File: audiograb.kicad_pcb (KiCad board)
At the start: 4 copper layers, 166.6 x 68.9 mm, 105 parts, among them IC1 USB2244I-AEZG-06, J1 USB_C_Receptacle_USB2.0_16P, J10 TestPoint, J11 TestPoint, J12 TestPoint, J13 TestPoint, J14 TestPoint, J15 F32Q-1A7H1-11022, J16 MEM2075-00-140-01-A, J17 5V_out, J18 3V7_in, J19 3V3_in, J2 SAM10346-ND, J3 Conn_02x20_Odd_Even, J4 CONMHF1-SMD-G-T, J5 CONMHF1-SMD-G-T, J6 TestPoint, J7 TestPoint, J8 TestPoint, J9 TestPoint, M1 ComputeModule5-CM5, P1 SF72S006VBAR2500, Q1 Q_PMOS_GSD, SW1 1825910-6, U1 RC7620_1104625, U10 CD4043BDR, U11 TPS22919DCKR, U12 IP4220CZ6F, U2 NX3008NBKW_115, U3 NX3008NBKW_115, U4 NX3008NBKW_115, U5 NX3008NBKW_115, U6 NX3008NBKW_115, U7 NX3008NBKW_115, U8 MAX4996LETG_

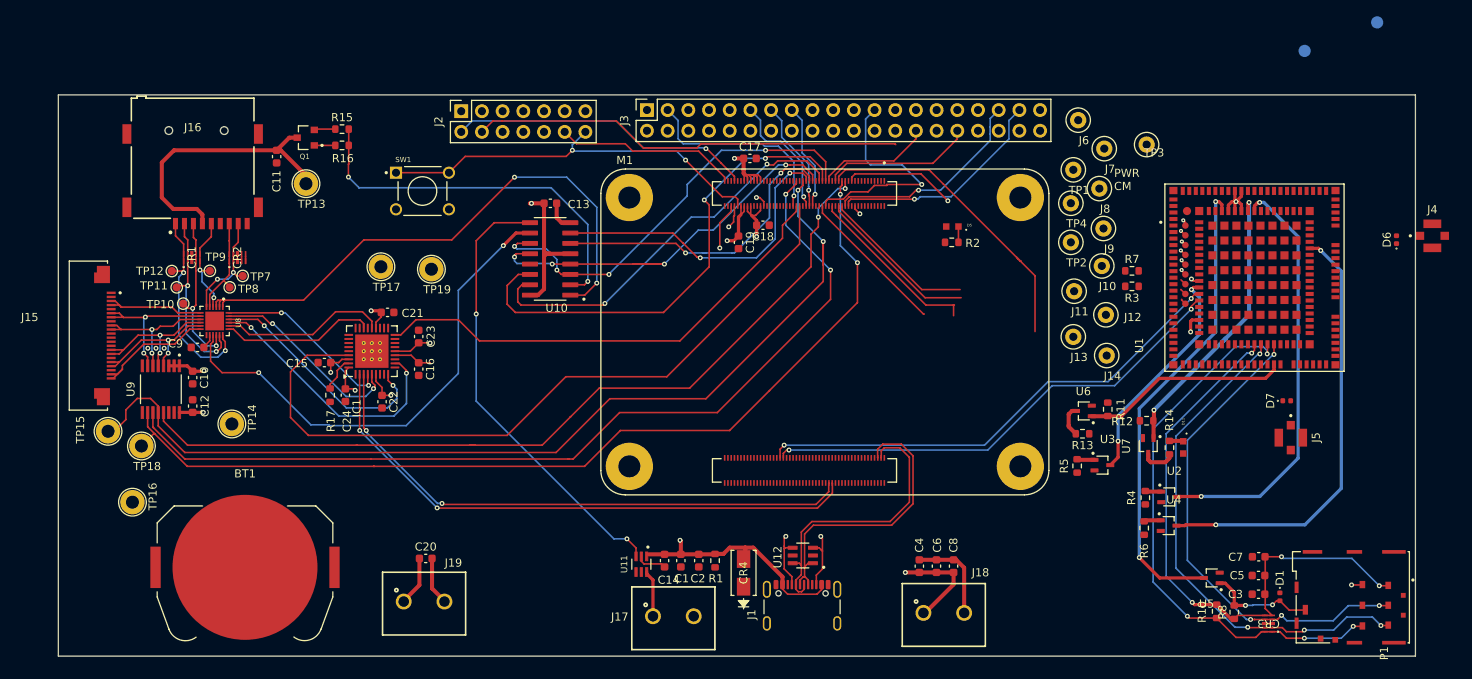
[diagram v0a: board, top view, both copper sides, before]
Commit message: partially route the powerlines
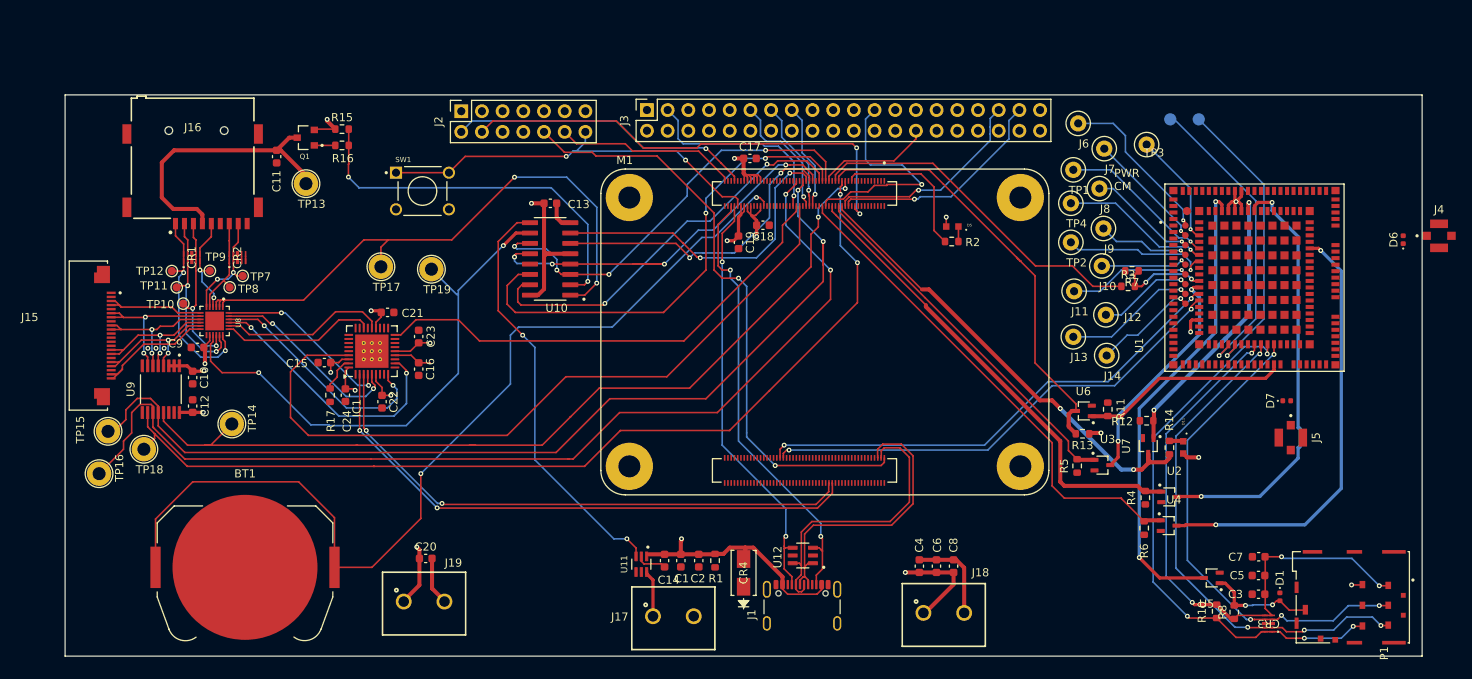
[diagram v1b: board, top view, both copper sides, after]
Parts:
- moved TP6 24.9 mm to (217.5, 24.0)
- moved TP5 18.5 mm to (214.0, 24.0)
- moved TP16 5.39 mm to (82.5, 67.5)
- moved D6 0.82 mm to (242.6, 38.8)
- moved J4 0.82 mm to (247.0, 38.3)
- moved TP18 0.50 mm to (88.0, 64.5)
- moved R3 0.48 mm to (208.8, 44.5), turned to 0 degrees
- moved J6 0.40 mm to (202.7, 24.5)
- moved R2 0.10 mm to (187.2, 39.0)
- turned R7 to 180 degrees
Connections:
- C10 pad 1: +1V8 -> +1V8_CM5
- J3 pad 29: unconnected-(J3-Pin_29-Pad29) -> +1V8_CM5
- J3 pad 32: /compute-module/GPIO12 -> unconnected-(J3-Pin_32-Pad32)
- J3 pad 33: +1V8 -> unconnected-(J3-Pin_33-Pad33)
- M1 pad 31: /compute-module/GPIO12 -> /Wake
- R3 pad 1: /modem/WAKE -> /Wake
- U9 pad 1: +1V8 -> +1V8_CM5
- U9 pad 2: +1V8 -> +1V8_CM5
- U9 pad 3: +1V8 -> +1V8_CM5
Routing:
- net +3V3: track 31.9 -> 287.5 mm, vias 2 -> 7
- net +1V8_CM5: track 6.67 -> 150.3 mm, vias 1 -> 2
- net +3V3_CM5: track 23.6 -> 149.6 mm, vias 5 -> 6
- net /compute-module/VBAT: track 1.65 -> 116.7 mm, vias 1 -> 2
- net /compute-module/USB_OTG_ID: track 0.00 -> 74.4 mm, vias 0 -> 2
- net VBAT_BB: track 22.7 -> 90.7 mm
- net +5V: track 39.0 -> 100.8 mm
- net /Wake: track 0.00 -> 42.7 mm
- net /CC1: track 10.3 -> 51.9 mm
- net /CC2: track 13.4 -> 54.7 mm
- net /MODEM_BOOT_MODE: track 20.4 -> 61.1 mm
- net Net-(U1A-SYS_CLK): track 0.00 -> 37.4 mm, vias 0 -> 1
- net Net-(U1A-SLEEP_CLK): track 0.00 -> 35.9 mm, vias 0 -> 1
- net /MODEM_POWER_ON_N: track 23.7 -> 58.4 mm
- net /MODEM_TX_ON: track 23.2 -> 56.9 mm, vias 0 -> 2
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
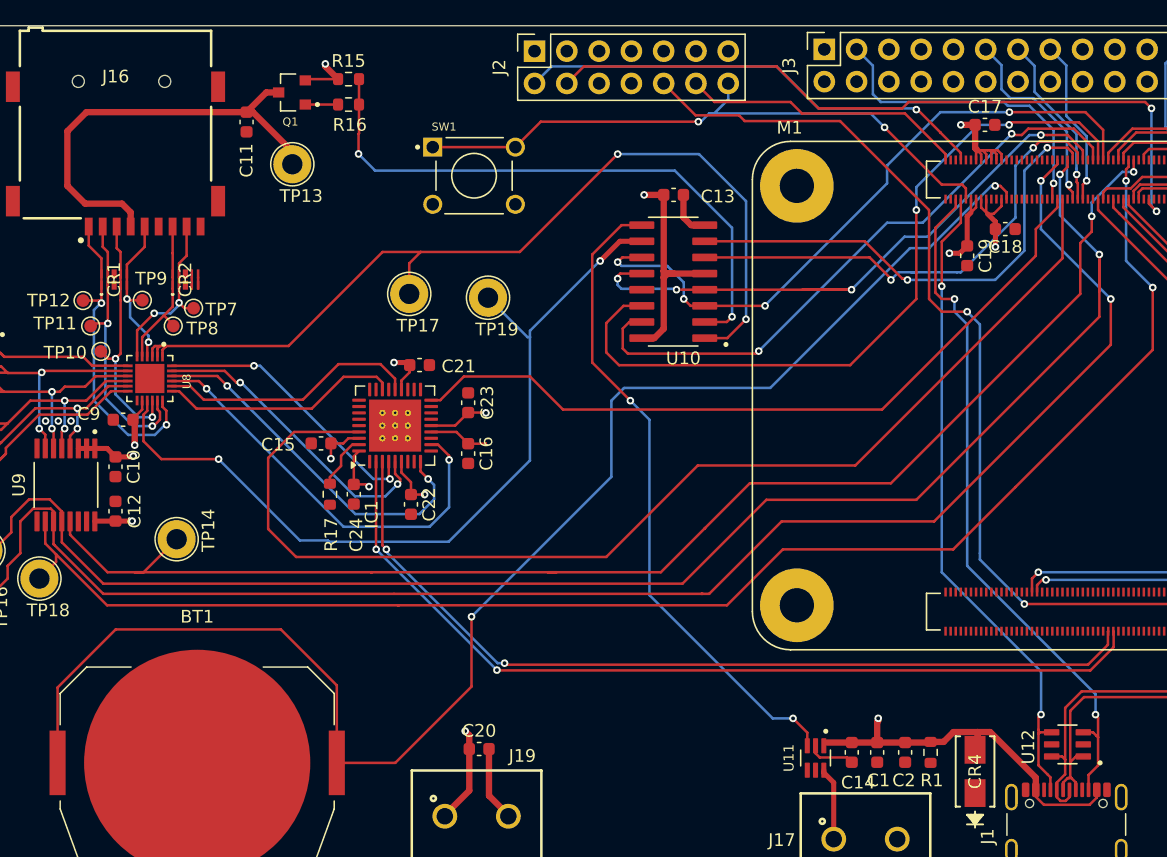
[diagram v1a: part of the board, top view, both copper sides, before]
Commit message: powergrid complete, still missing antennas
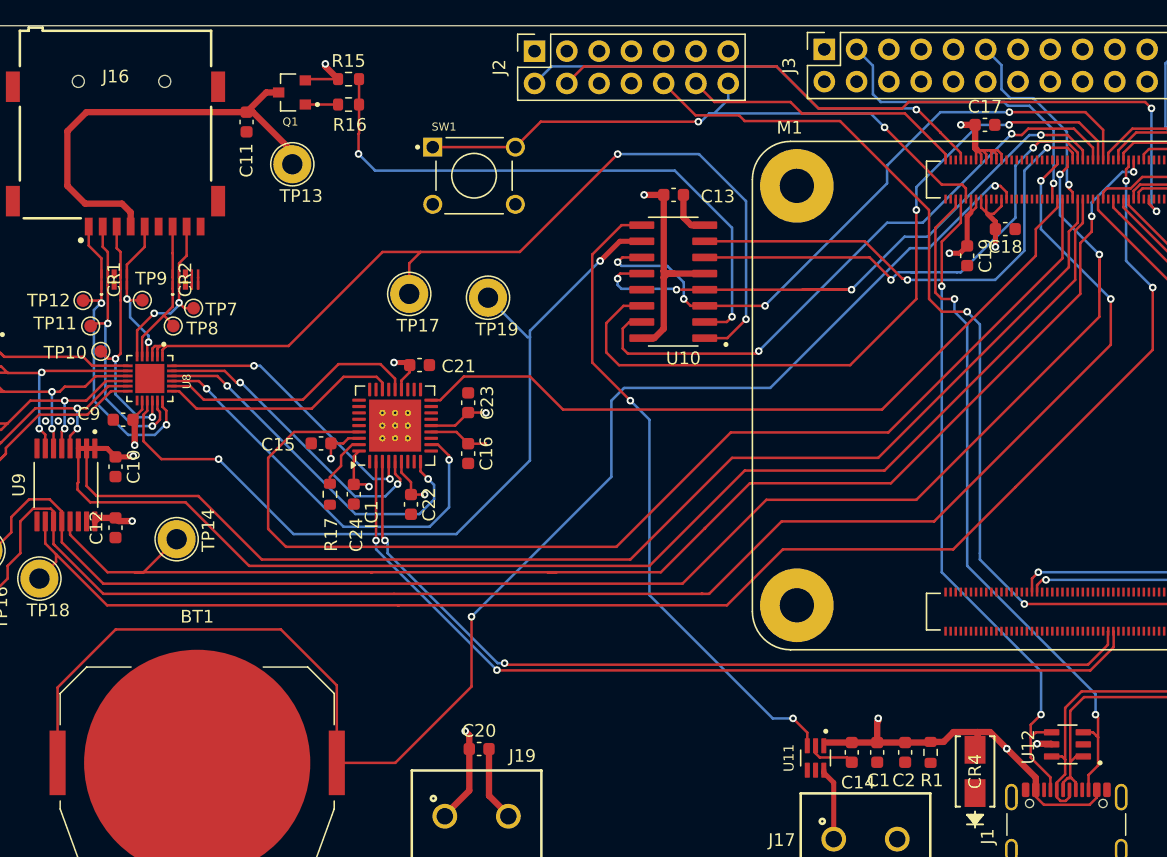
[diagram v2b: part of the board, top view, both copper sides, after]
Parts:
- moved C12 1.30 mm to (94.0, 60.5), turned to -90 degrees
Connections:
- J3 pad 13: /compute-module/GPIO27 -> unconnected-(J3-Pin_13-Pad13)
- J3 pad 15: /compute-module/GPIO22 -> unconnected-(J3-Pin_15-Pad15)
- M1 pad 46: /compute-module/GPIO22 -> /2DIR
- M1 pad 48: /compute-module/GPIO27 -> /1DIR
- U9 pad 2: +1V8_CM5 -> /1DIR
- U9 pad 3: +1V8_CM5 -> /2DIR
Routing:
- net /2DIR: track 0.00 -> 99.8 mm
- net /1DIR: track 0.00 -> 97.4 mm
- net +3V3_CM5: track 149.6 -> 177.9 mm
- net /compute-module/GPIO27: track 13.7 -> 0.00 mm, vias 1 -> 0
- net /compute-module/GPIO22: track 13.1 -> 0.00 mm, vias 1 -> 0
- net +5V: track 100.8 -> 104.5 mm, vias 2 -> 4
- net /CC1: track 51.9 -> 53.1 mm
- net /GPCLK: track 91.4 -> 90.7 mm

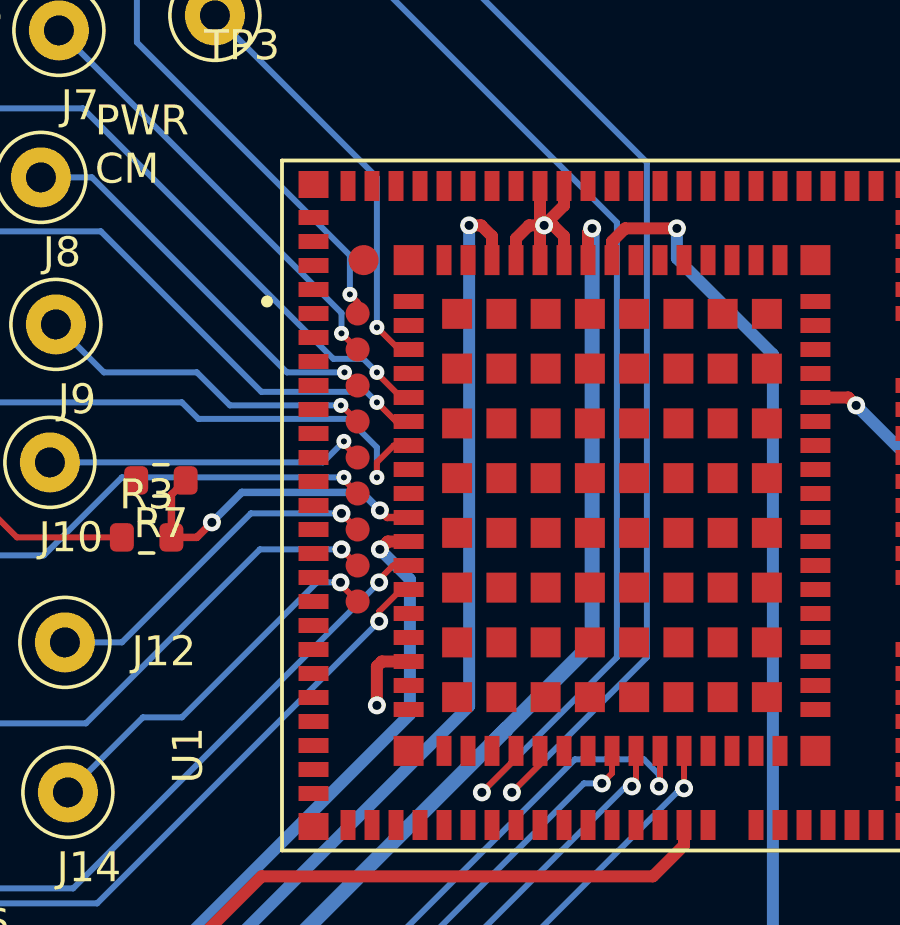
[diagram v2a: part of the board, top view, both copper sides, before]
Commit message: Modem power supply hsould be correct
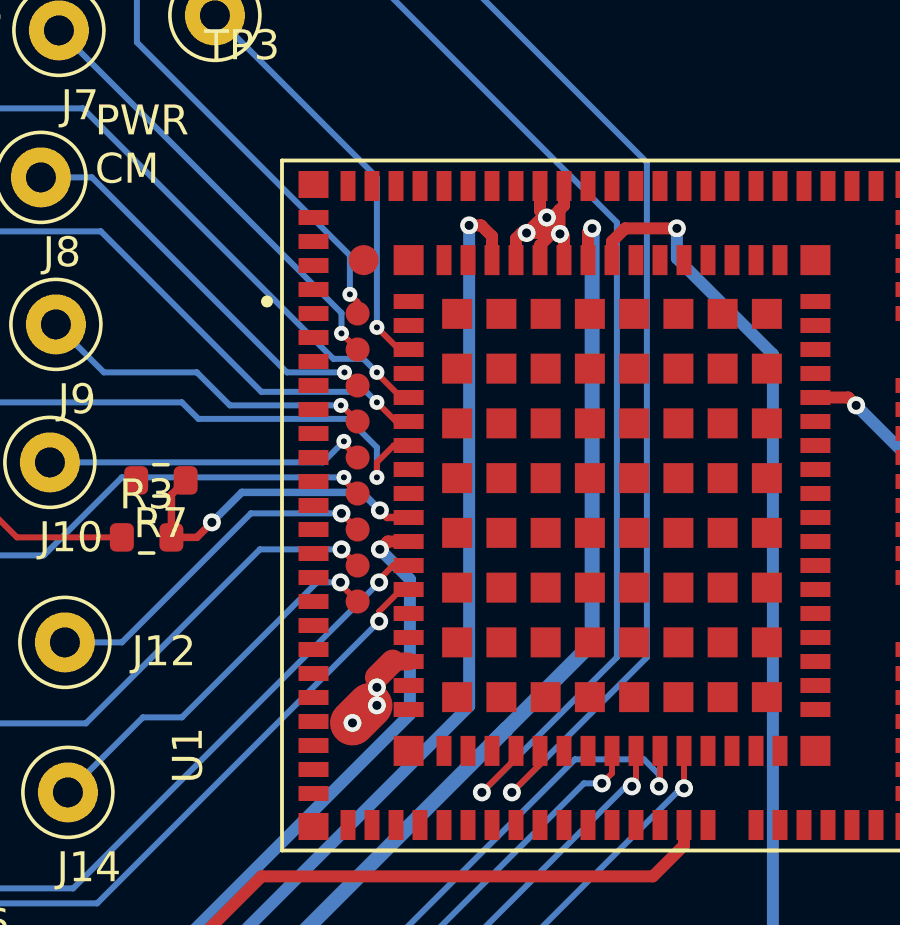
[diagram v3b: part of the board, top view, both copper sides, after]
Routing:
- net VBAT_BB: track 90.7 -> 94.4 mm, vias 3 -> 7

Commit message: mjeu
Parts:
- added REF**: Untitled, Untitled, F.Cu at (228.3, 57.2)
- J4, J5: value CONMHF1-SMD-G-T -> EMPCB.SMAFSTJ.B.HT; footprint CONMHF1-SMD-G-T:LINX_CONMHF1-SMD-G-T -> EMPCB.SMAFSTJ.B.HT:TAOGLAS_EMPCB.SMAFSTJ.B.HT
- moved J5 13.4 mm to (242.1, 63.7), turned to 90 degrees
- moved J4 4.66 mm to (242.3, 38.2)
- moved D6 4.30 mm to (238.3, 38.7)
- moved TP17 2.71 mm to (114.4, 42.3)
- moved TP19 2.20 mm to (125.2, 43.5)
- moved D7 0.56 mm to (227.8, 58.3)
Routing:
- net Net-(D7-A2): track 0.00 -> 22.7 mm
- net Net-(D6-A2): track 0.00 -> 7.44 mm
- net /compute-module/GPIO11: track 28.0 -> 22.9 mm
- net Net-(U10-Q3): track 65.7 -> 63.2 mm
- net VBAT_BB: track 94.4 -> 96.3 mm
- net Net-(U10-Q4): track 73.9 -> 72.5 mm
- net +3V3: track 287.7 -> 286.9 mm
- net +1V8_CM5: track 150.3 -> 149.7 mm
- net /MODEM_POWER_ON_N: track 58.4 -> 57.8 mm
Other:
- board size 166.6 x 68.9 mm -> 166.6 x 69.7 mm

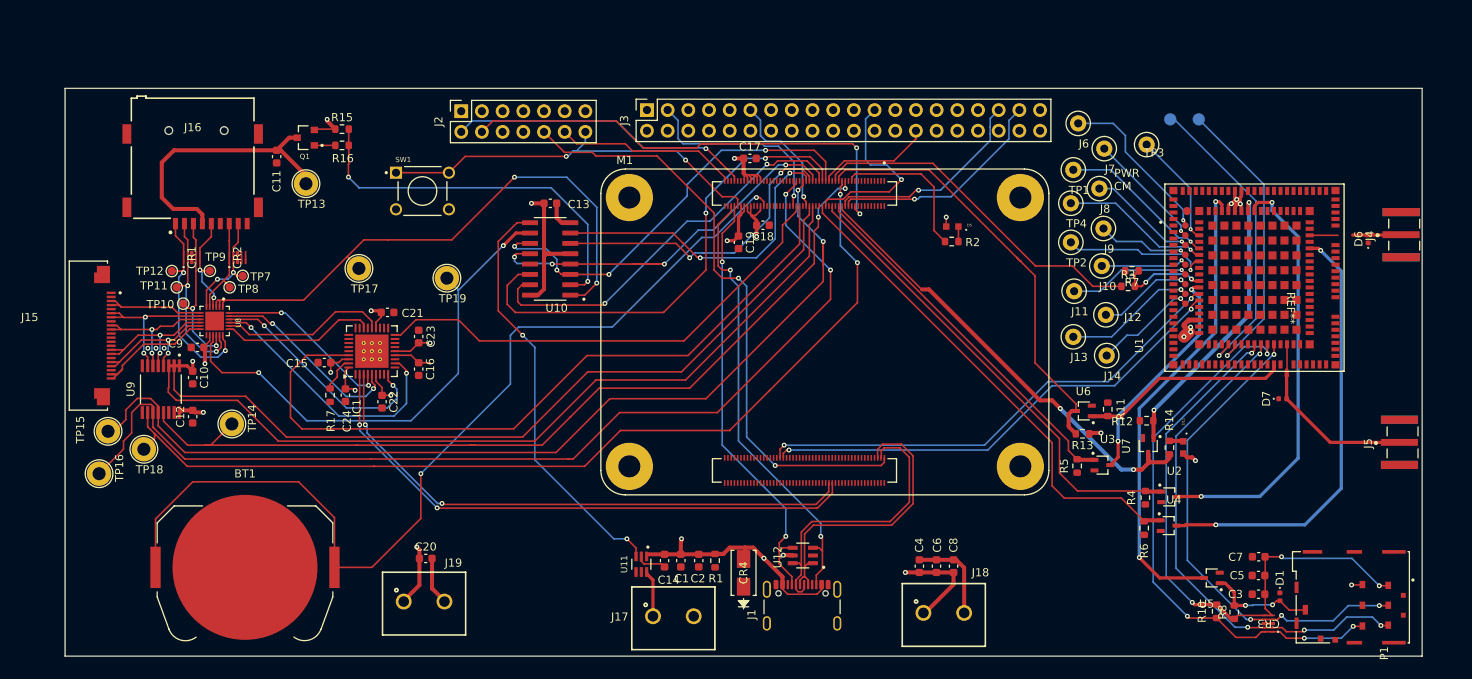
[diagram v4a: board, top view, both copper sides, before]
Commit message: power supply completed and stated on vias along the edge
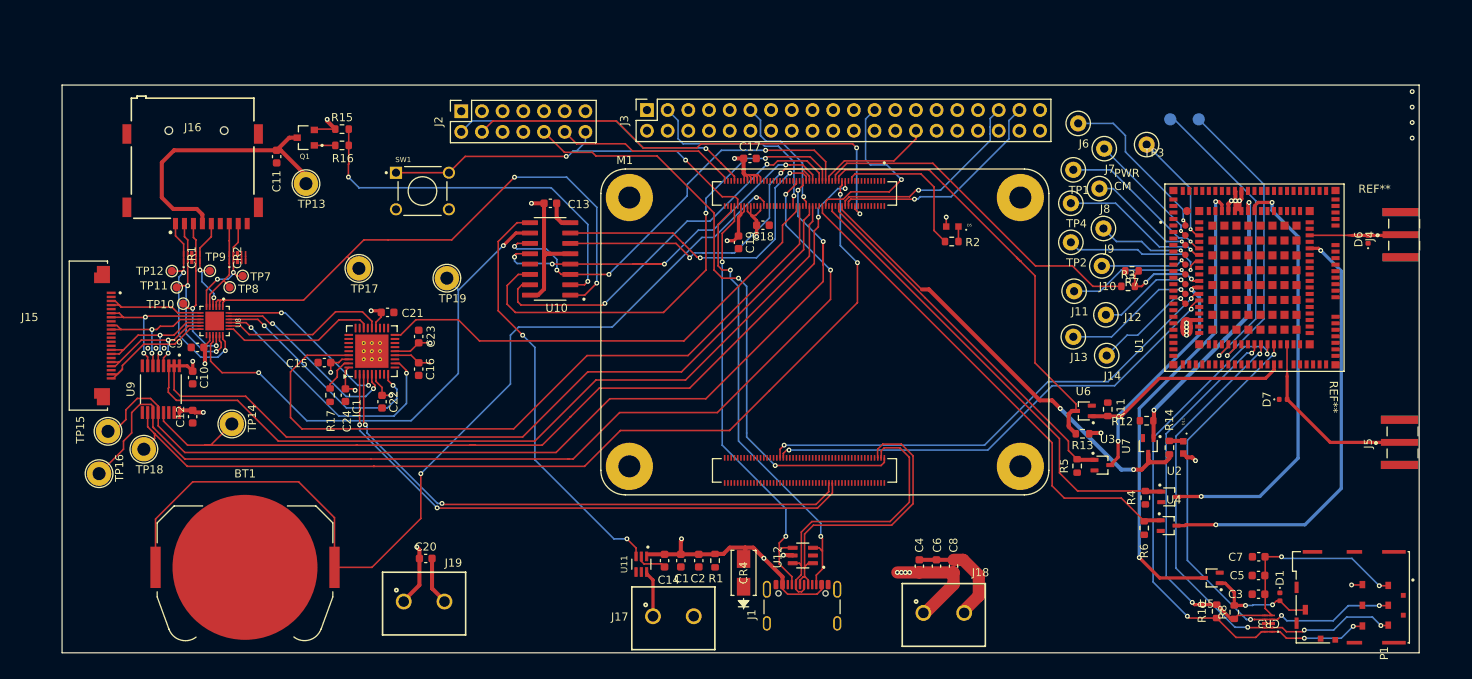
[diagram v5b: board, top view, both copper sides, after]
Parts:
- added REF**: , Untitled, F.Cu at (238.3, 38.2)
- REF**: value Untitled -> (none)
- moved D7 0.10 mm to (227.9, 58.4)
- moved REF** 0.09 mm to (228.3, 57.3)
- moved D6 0.05 mm to (238.3, 38.7)
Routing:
- net GND: track 26.8 -> 28.8 mm
- net Net-(D6-A2): track 7.44 -> 9.26 mm
- net VBAT_BB: track 96.3 -> 95.3 mm, vias 7 -> 11
- net (no net): vias 0 -> 4

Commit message: earth plane, vias, connector ect
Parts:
- added MP1: WA-SMSI_9774XXX151, WA-SMSI_9774XXX151:WA-SMSI_9774030151, F.Cu at (195.7, 33.6)
- added MP2: WA-SMSI_9774XXX151, WA-SMSI_9774XXX151:WA-SMSI_9774030151, F.Cu at (147.6, 33.6)
- added MP3: WA-SMSI_9774XXX151, WA-SMSI_9774XXX151:WA-SMSI_9774030151, F.Cu at (147.6, 66.7)
- added MP4: WA-SMSI_9774XXX151, WA-SMSI_9774XXX151:WA-SMSI_9774030151, F.Cu at (195.6, 66.6)
- added TP20: TestPoint, TestPoint:TestPoint_Pad_D1.0mm, B.Cu at (170.4, 33.8)
- added TP21: TestPoint, TestPoint:TestPoint_Pad_D1.0mm, B.Cu at (166.7, 38.4)
- moved C20 2.04 mm to (122.6, 80.0)
- moved TP18 1.75 mm to (88.9, 66.0)
- moved J19 1.60 mm to (122.4, 84.8)
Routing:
- net GND: track 28.8 -> 60.9 mm, vias 4 -> 55
- net +3V3: track 286.9 -> 293.4 mm
- net /SD_SWITCH_DISABLE: track 50.1 -> 45.7 mm
- net +5V: track 104.5 -> 106.9 mm, vias 4 -> 6
- net +1V8_CM5: track 149.7 -> 147.7 mm
- net Net-(U1A-UART1_DTR): track 18.5 -> 16.7 mm
- net /SD5: track 125.3 -> 127.0 mm
- net Net-(IC1-VDD18): track 4.71 -> 3.30 mm
- net Net-(IC1-VDD18PLL): track 3.58 -> 2.38 mm, vias 1 -> 0
- net +3V3_CM5: track 177.9 -> 177.0 mm
- net /sd-interface/SD-pin7: track 24.3 -> 24.9 mm
- net /compute-module/USB_OTG_ID: track 74.4 -> 75.0 mm
- net /SD3: track 119.3 -> 118.7 mm
- added copper zone on F.Cu, net GND
- added copper zone on In1.Cu, net GND
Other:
- board size 166.6 x 69.7 mm -> 167 x 69.7 mm
- board text added: "CM POWER"
- board text added: "VOUT"
